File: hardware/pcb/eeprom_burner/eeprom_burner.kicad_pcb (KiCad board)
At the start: 2 copper layers, 68.6 x 53.3 mm, 23 parts, among them J1 Conn_01x08, J2 Conn_01x08, J3 Conn_01x08, J4 Conn_01x06, P1 Power, P2 Analog, P3 Digital, P4 Digital, P5 CONN_01X01, P6 CONN_01X01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

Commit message: Update board
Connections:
- P3 pad 2: Net-(P3-Pad2) -> ~OE~
- U3 pad 20: GND -> E0
- U3 pad 22: A15 -> ~OE~
- U4 pad 23: GND -> E1
- U4 pad 25: A15 -> ~OE~

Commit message: Power net class
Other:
- net class PWR added: clearance 0.2, trace_width 0.5, via_dia 0.6, via_drill 0.4
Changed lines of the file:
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@@
     (uvia_dia 0.3)
     (uvia_drill 0.1)
-    (add_net +5V)
     (add_net A0)
     (add_net A1)
@@
     (add_net E4)
     (add_net E5)
-    (add_net GND)
     (add_net LATCH)
     (add_net MISO)
@@
     (add_net ~WE~)
   )
+  (net_class PWR ""
+    (clearance 0.2)
+    (trace_width 0.5)
+    (via_dia 0.6)
+    (via_drill 0.4)
+    (uvia_dia 0.3)
+    (uvia_drill 0.1)
+    (add_net +5V)
+    (add_net GND)
+  )
   (module Connector_PinSocket_2.54mm:PinSocket_1x08_P2.54mm_Vertical (layer F.Cu)

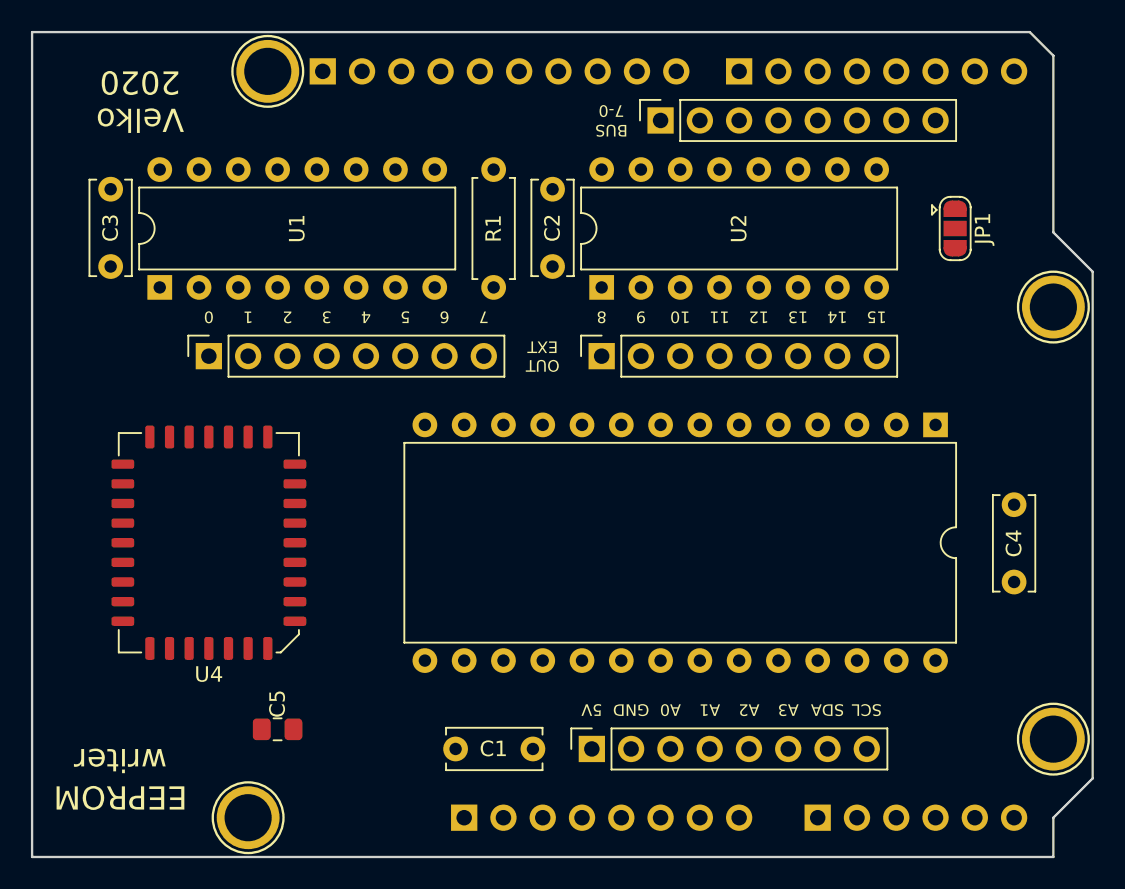
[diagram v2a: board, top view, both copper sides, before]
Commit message: Import autorouted
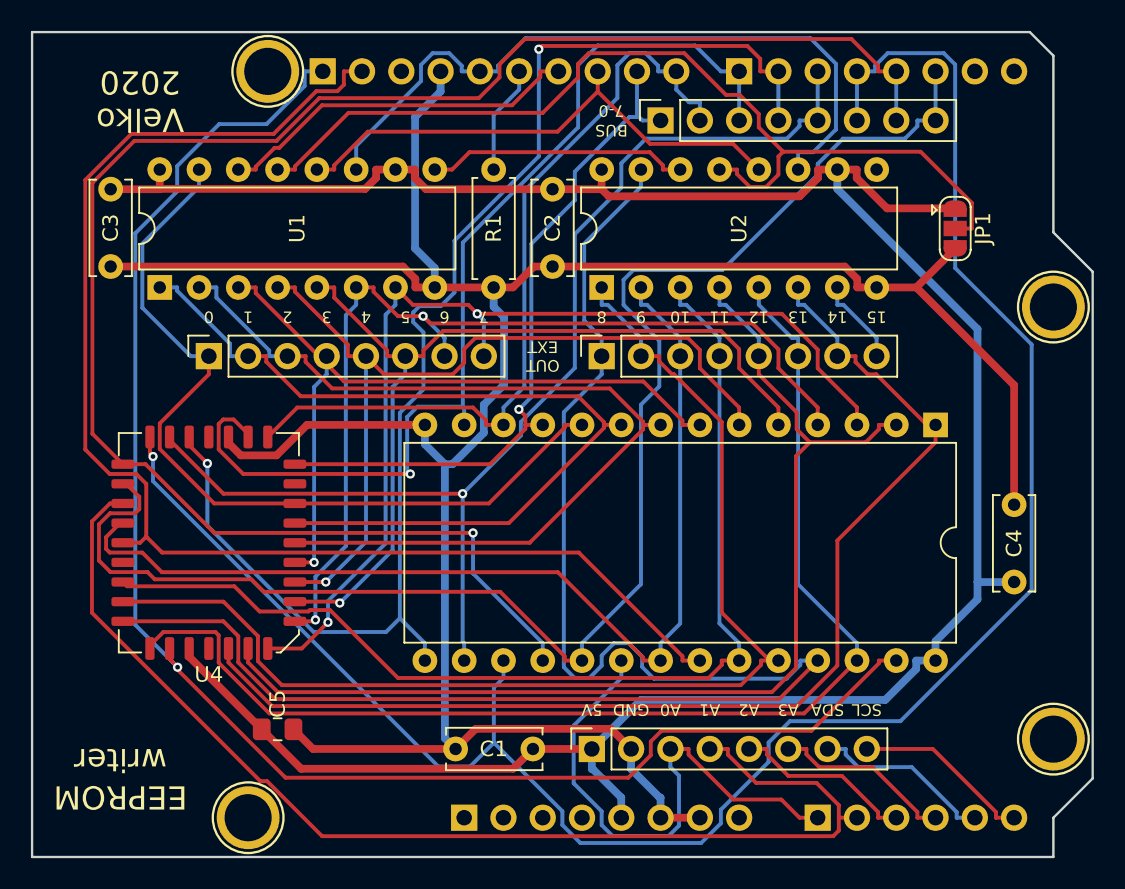
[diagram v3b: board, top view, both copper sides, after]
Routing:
- net GND: track 0.00 -> 170.7 mm
- net +5V: track 0.00 -> 160.7 mm
- net D5: track 0.00 -> 131.4 mm, vias 0 -> 1
- net D6: track 0.00 -> 114.2 mm, vias 0 -> 1
- net A8: track 0.00 -> 104.2 mm
- net ~WE~: track 0.00 -> 101.9 mm, vias 0 -> 1
- net D7: track 0.00 -> 97.5 mm
- net ~OE~: track 0.00 -> 88.0 mm
- net D3: track 0.00 -> 87.1 mm, vias 0 -> 2
- net A13: track 0.00 -> 77.9 mm
- net A9: track 0.00 -> 76.0 mm
- net E1: track 0.00 -> 75.7 mm
- net A14: track 0.00 -> 74.9 mm
- net D4: track 0.00 -> 74.3 mm, vias 0 -> 1
- net A12: track 0.00 -> 71.6 mm
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
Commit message: Manual touch-up
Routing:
- net +5V: track 160.7 -> 159.5 mm
- net A5: track 57.7 -> 56.9 mm
- net D1: track 52.0 -> 51.2 mm
- net A14: track 74.9 -> 75.6 mm
- net GND: track 170.7 -> 170.0 mm
- net ~OE~: track 88.0 -> 87.3 mm
- net A4: track 55.6 -> 55.0 mm

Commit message: Add copper pour
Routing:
- added copper zone on F.Cu, net +5V
- added copper zone on B.Cu, net GND
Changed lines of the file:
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@@
   (layers
     (0 F.Cu signal)
-    (31 B.Cu signal)
+    (31 B.Cu signal hide)
     (32 B.Adhes user hide)
     (33 F.Adhes user hide)
@@
     (42 Eco1.User user hide)
     (43 Eco2.User user hide)
-    (44 Edge.Cuts user hide)
+    (44 Edge.Cuts user)
     (45 Margin user hide)
     (46 B.CrtYd user hide)
@@
   (segment (start 118.3805 105.651) (end 119.4094 106.6799) (width 0.25) (layer F.Cu) (net 57))
   (segment (start 119.4094 106.6799) (end 147.1929 106.6799) (width 0.25) (layer F.Cu) (net 57))
+  (zone (net 2) (net_name GND) (layer B.Cu) (hatch edge 0.508)
+    (connect_pads (clearance 0.208))
+    (min_thickness 0.254)
+    (fill yes (arc_segments 16) (thermal_gap 0.508) (thermal_bridge_width 0.508))
+    (polygon
+      (pts
+        (xy 110.998 126.365) (xy 179.578 126.365) (xy 179.578 73.025) (xy 110.998 73.025)
+      )
+    )
+  )
+  (zone (net 1) (net_name +5V) (layer F.Cu) (hatch edge 0.508)
+    (connect_pads (clearance 0.208))
+    (min_thickness 0.254)
+    (fill yes (arc_segments 16) (thermal_gap 0.508) (thermal_bridge_width 0.508))
+    (polygon
+      (pts
+        (xy 110.998 126.365) (xy 179.578 126.365) (xy 179.578 73.025) (xy 110.998 73.025)
+      )
+    )
+  )
 )

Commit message: Add silk
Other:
- board text added: "594"
- board text added: "595"
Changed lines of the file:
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@@
   (general
     (thickness 1.6)
-    (drawings 55)
+    (drawings 57)
     (tracks 604)
     (zones 0)
@@
   (layers
     (0 F.Cu signal)
-    (31 B.Cu signal hide)
+    (31 B.Cu signal)
     (32 B.Adhes user hide)
     (33 F.Adhes user hide)
@@
     (37 F.SilkS user)
     (38 B.Mask user hide)
-    (39 F.Mask user hide)
+    (39 F.Mask user)
     (40 Dwgs.User user hide)
     (41 Cmts.User user hide)
@@
     (tags "solder jumper open")
     (attr virtual)
-    (fp_text reference JP1 (at 0 -1.8 270) (layer F.SilkS)
+    (fp_text reference JP1 (at 0 -1.8 270) (layer F.Fab)
       (effects (font (size 1 1) (thickness 0.15)))
     )
@@
     )
   )
+  (gr_text 595 (at 170.688 88.9 180) (layer F.SilkS)
+    (effects (font (size 1 1) (thickness 0.125)))
+  )
+  (gr_text 594 (at 170.688 82.55 180) (layer F.SilkS)
+    (effects (font (size 1 1) (thickness 0.125)))
+  )
   (gr_text "EEPROM\nwriter" (at 116.713 121.285 180) (layer F.SilkS)
